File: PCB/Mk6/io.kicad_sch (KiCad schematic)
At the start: 7 parts, among them J10 PortA: 5V PA0 PA1 PA2 PA3 PA4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, J26 Conn_01x12, J27 Conn_01x12, J4 PortB: 5V PB0 PB1 PB2 PB3 PB4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, U25 74LS573, U26 74LS574, U6 R6522

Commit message: save point
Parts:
- added J5: DISPLAY, Connector_PinSocket_2.54mm:PinSocket_1x32_P2.54mm_Vertical, symbol Connector_Generic:Conn_01x32
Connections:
- net +5V: now also J5.18 (Pin_18)
- net A0: now also J5.20 (Pin_20)
- net A1: now also J5.21 (Pin_21)
- net A2: now also J5.22 (Pin_22)
- net A3: now also J5.23 (Pin_23)
- net Clk2: now also J5.7 (Pin_7)
- net D0: now also J5.10 (Pin_10)
- net D1: now also J5.11 (Pin_11)
- net D2: now also J5.12 (Pin_12)
- net D3: now also J5.13 (Pin_13)
- net D4: now also J5.14 (Pin_14)
- net D5: now also J5.15 (Pin_15)
- net D6: now also J5.16 (Pin_16)
- net D7: now also J5.17 (Pin_17)
- net GND: now also J5.19 (Pin_19)
- net R~{W}: now also J5.4 (Pin_4)
- net ~{IRQ}: now also J5.8 (Pin_8)
- net ~{RST}: now also J5.5 (Pin_5)
- net ~{OUT}: now reaches J27.10 (Pin_10), U26.11 (Cp)
- net ~{KEY}: now reaches J26.10 (Pin_10), U25.1 (~{OE})
- new net A10: J5.30 (Pin_30)
- new net A11: J5.31 (Pin_31)
- new net A12: J5.32 (Pin_32)
- new net A4: J5.24 (Pin_24)
- new net A5: J5.25 (Pin_25)
- new net A6: J5.26 (Pin_26)
- new net A7: J5.27 (Pin_27)
- new net A8: J5.28 (Pin_28)
- new net A9: J5.29 (Pin_29)
- new net DISP: J5.1 (Pin_1)
- new net RDY: J5.6 (Pin_6)
- new net ~{NMI}: J5.9 (Pin_9)
- new net ~{RD}: J5.3 (Pin_3)
- new net ~{WR}: J5.2 (Pin_2)

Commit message: save
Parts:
- added R3, R5: R_Small_US, Resistor_THT:R_Axial_DIN0204_L3.6mm_D1.6mm_P7.62mm_Horizontal, symbol Device:R_Small_US
- J7: renamed from J26; value Conn_01x12 -> Input Port; footprint Connector_PinHeader_1.00mm:PinHeader_1x12_P1.00mm_Vertical -> Connector_PinHeader_2.54mm:PinHeader_1x12_P2.54mm_Vertical
- J8: renamed from J27; value Conn_01x12 -> Output Port; footprint Connector_PinHeader_1.00mm:PinHeader_1x12_P1.00mm_Vertical -> Connector_PinHeader_2.54mm:PinHeader_1x12_P2.54mm_Vertical
- renumbered J5 to J10, J10 to J5, J4 to J6, U6 to U10, U25 to U11, U26 to U12
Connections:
- net +5V: now also R5.1
- net A0: now also J10.32 (Pin_32); no longer J10.20 (Pin_20)
- net A1: now also J10.31 (Pin_31); no longer J10.21 (Pin_21)
- net A10: now also J10.22 (Pin_22); no longer J10.30 (Pin_30)
- net A11: now also J10.21 (Pin_21); no longer J10.31 (Pin_31)
- net A12: now also J10.20 (Pin_20); no longer J10.32 (Pin_32)
- net A2: now also J10.30 (Pin_30); no longer J10.22 (Pin_22)
- net A3: now also J10.29 (Pin_29); no longer J10.23 (Pin_23)
- net A4: now also J10.28 (Pin_28); no longer J10.24 (Pin_24)
- net A5: now also J10.27 (Pin_27); no longer J10.25 (Pin_25)
- net A7: now also J10.25 (Pin_25); no longer J10.27 (Pin_27)
- net A8: now also J10.24 (Pin_24); no longer J10.28 (Pin_28)
- net A9: now also J10.23 (Pin_23); no longer J10.29 (Pin_29)
- net GND: now also R3.1
- net ~{OutEn}: now reaches J8.11 (Pin_11), U12.1 (~{OE})
- net ~{OutEn}: now also R3.2
- net ~{Hold}/Follow: now reaches J7.11 (Pin_11), U11.11 (Load)
- net ~{Hold}/Follow: now also R5.2
- net ~{KEY} renamed ~{IN}
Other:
- moved on the sheet: J10

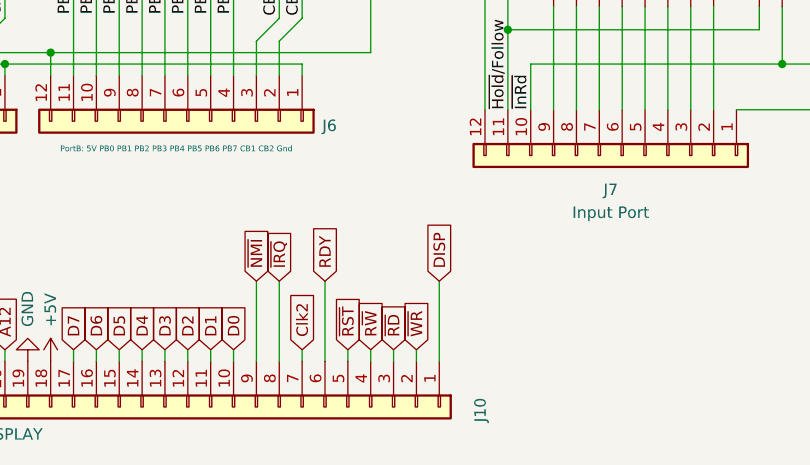
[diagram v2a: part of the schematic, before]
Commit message: all done, pre-clk div
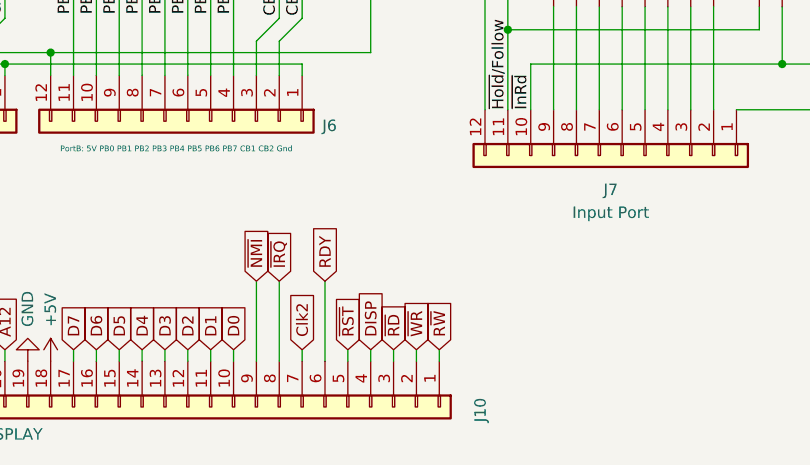
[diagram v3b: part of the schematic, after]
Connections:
- net DISP: now also J10.4 (Pin_4); no longer J10.1 (Pin_1)
- net R~{W}: now also J10.1 (Pin_1); no longer J10.4 (Pin_4)

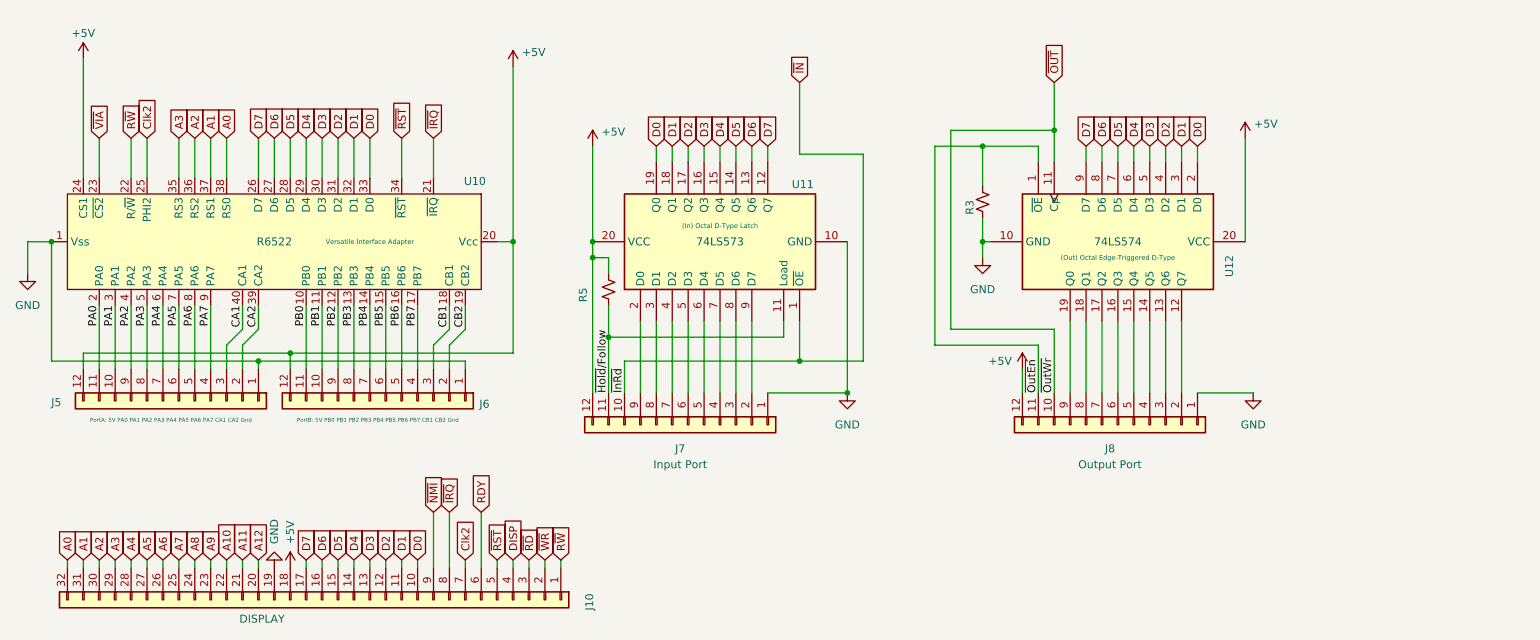
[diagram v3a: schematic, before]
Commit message: Added 3-8 IO, extra GAL out, attachment point for !RAM
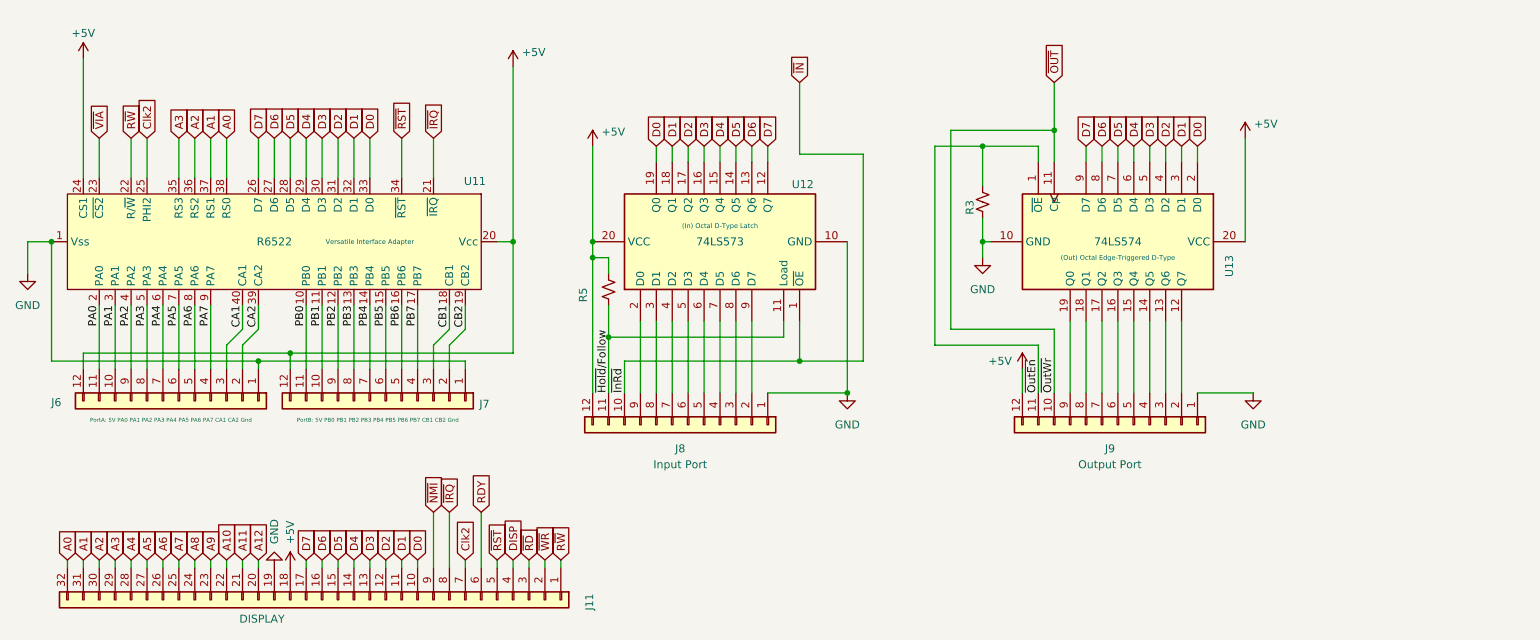
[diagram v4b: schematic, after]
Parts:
- renumbered J10 to J11, J5 to J6, J6 to J7, J7 to J8, J8 to J9, U10 to U11, U11 to U12, U12 to U13
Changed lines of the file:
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@@
 		(dnp no)
 		(fields_autoplaced yes)
-		(property "Reference" "J8"
+		(property "Reference" "J9"
 			(at 191.77 91.44 90)
 			(effects
@@
 			(project ""
 				(path "/d41350ce-2040-418d-ae11-f076a5474776/991bdc6c-c9f2-46dc-9106-bb77d701fb18"
-					(reference "J8")
+					(reference "J9")
 					(unit 1)
 				)
@@
 		(dnp no)
 		(fields_autoplaced yes)
-		(property "Reference" "U12"
+		(property "Reference" "U13"
 			(at 210.82 60.5633 0)
 			(effects
@@
 			(project ""
 				(path "/d41350ce-2040-418d-ae11-f076a5474776/991bdc6c-c9f2-46dc-9106-bb77d701fb18"
-					(reference "U12")
+					(reference "U13")
 					(unit 1)
 				)
@@
 		(dnp no)
 		(fields_autoplaced yes)
-		(property "Reference" "#PWR037"
+		(property "Reference" "#PWR038"
 			(at 60.96 114.3 0)
 			(effects
@@
 			(project "Mk6"
 				(path "/d41350ce-2040-418d-ae11-f076a5474776/991bdc6c-c9f2-46dc-9106-bb77d701fb18"
-					(reference "#PWR037")
+					(reference "#PWR038")
 					(unit 1)
 				)
@@
 		(on_board yes)
 		(dnp no)
-		(property "Reference" "J6"
+		(property "Reference" "J7"
 			(at 91.948 84.328 90)
 			(effects
@@
 			(project "Mk6"
 				(path "/d41350ce-2040-418d-ae11-f076a5474776/991bdc6c-c9f2-46dc-9106-bb77d701fb18"
-					(reference "J6")
+					(reference "J7")
 					(unit 1)
 				)
@@
 		(on_board yes)
 		(dnp no)
-		(property "Reference" "#PWR023"
+		(property "Reference" "#PWR024"
 			(at 27.94 33.02 0)
 			(effects
@@
 			(project "Mk6"
 				(path "/d41350ce-2040-418d-ae11-f076a5474776/991bdc6c-c9f2-46dc-9106-bb77d701fb18"
-					(reference "#PWR023")
+					(reference "#PWR024")
 					(unit 1)
 				)
@@
 		(on_board yes)
 		(dnp no)
-		(property "Reference" "#PWR024"
+		(property "Reference" "#PWR025"
 			(at 96.52 34.29 0)
 			(effects
@@
 			(project "Mk6"
 				(path "/d41350ce-2040-418d-ae11-f076a5474776/991bdc6c-c9f2-46dc-9106-bb77d701fb18"
-					(reference "#PWR024")
+					(reference "#PWR025")
 					(unit 1)
 				)
@@
 		(on_board yes)
 		(dnp no)
-		(property "Reference" "#PWR025"
+		(property "Reference" "#PWR026"
 			(at 213.36 45.72 0)
 			(effects
@@
 			(project "Mk6"
 				(path "/d41350ce-2040-418d-ae11-f076a5474776/991bdc6c-c9f2-46dc-9106-bb77d701fb18"
-					(reference "#PWR025")
+					(reference "#PWR026")
 					(unit 1)
 				)
@@
 		(dnp no)
 		(fields_autoplaced yes)
-		(property "Reference" "#PWR030"
+		(property "Reference" "#PWR031"
 			(at 19.05 69.85 0)
 			(effects
@@
 			(project "Mk6"
 				(path "/d41350ce-2040-418d-ae11-f076a5474776/991bdc6c-c9f2-46dc-9106-bb77d701fb18"
-					(reference "#PWR030")
+					(reference "#PWR031")
 					(unit 1)
 				)
@@
 		(on_board yes)
 		(dnp no)
-		(property "Reference" "#PWR027"
+		(property "Reference" "#PWR028"
 			(at 109.22 46.99 0)
 			(effects
@@
 			(project "Mk6"
 				(path "/d41350ce-2040-418d-ae11-f076a5474776/991bdc6c-c9f2-46dc-9106-bb77d701fb18"
-					(reference "#PWR027")
+					(reference "#PWR028")
 					(unit 1)
 				)
@@
 		(on_board yes)
 		(dnp no)
-		(property "Reference" "#PWR032"
+		(property "Reference" "#PWR033"
 			(at 177.8 82.55 0)
 			(effects
@@
 			(project "Mk6"
 				(path "/d41350ce-2040-418d-ae11-f076a5474776/991bdc6c-c9f2-46dc-9106-bb77d701fb18"
-					(reference "#PWR032")
+					(reference "#PWR033")
 					(unit 1)
 				)
@@
 		(dnp no)
 		(fields_autoplaced yes)
-		(property "Reference" "#PWR036"
+		(property "Reference" "#PWR037"
 			(at 58.42 104.14 0)
 			(effects
@@
 			(project "Mk6"
 				(path "/d41350ce-2040-418d-ae11-f076a5474776/991bdc6c-c9f2-46dc-9106-bb77d701fb18"
-					(reference "#PWR036")
+					(reference "#PWR037")
 					(unit 1)
 				)
@@
 		(dnp no)
 		(fields_autoplaced yes)
-		(property "Reference" "#PWR034"
+		(property "Reference" "#PWR035"
 			(at 149.86 88.9 0)
 			(effects
@@
 			(project "Mk6"
 				(path "/d41350ce-2040-418d-ae11-f076a5474776/991bdc6c-c9f2-46dc-9106-bb77d701fb18"
-					(reference "#PWR034")
+					(reference "#PWR035")
 					(unit 1)
 				)
@@
 		(on_board yes)
 		(dnp no)
-		(property "Reference" "U11"
+		(property "Reference" "U12"
 			(at 142.748 49.276 90)
 			(effects
@@
 			(project ""
 				(path "/d41350ce-2040-418d-ae11-f076a5474776/991bdc6c-c9f2-46dc-9106-bb77d701fb18"
-					(reference "U11")
+					(reference "U12")
 					(unit 1)
 				)
@@
 		(dnp no)
 		(fields_autoplaced yes)
-		(property "Reference" "#PWR028"
+		(property "Reference" "#PWR029"
 			(at 171.45 67.31 0)
 			(effects
@@
 			(project "Mk6"
 				(path "/d41350ce-2040-418d-ae11-f076a5474776/991bdc6c-c9f2-46dc-9106-bb77d701fb18"
-					(reference "#PWR028")
+					(reference "#PWR029")
 					(unit 1)
 				)
@@
 		(dnp no)
 		(fields_autoplaced yes)
-		(property "Reference" "#PWR035"
+		(property "Reference" "#PWR036"
 			(at 214.63 88.9 0)
 			(effects
@@
 			(project "Mk6"
 				(path "/d41350ce-2040-418d-ae11-f076a5474776/991bdc6c-c9f2-46dc-9106-bb77d701fb18"
-					(reference "#PWR035")
+					(reference "#PWR036")
 					(unit 1)
 				)
@@
 		(dnp no)
 		(fields_autoplaced yes)
-		(property "Reference" "J7"
+		(property "Reference" "J8"
 			(at 123.19 91.44 90)
 			(effects
@@
 			(project ""
 				(path "/d41350ce-2040-418d-ae11-f076a5474776/991bdc6c-c9f2-46dc-9106-bb77d701fb18"
-					(reference "J7")
+					(reference "J8")
 					(unit 1)
 				)
@@
 		(on_board yes)
 		(dnp no)
-		(property "Reference" "J10"
+		(property "Reference" "J11"
 			(at 108.712 114.554 0)
 			(effects
@@
 			(project "Mk6"
 				(path "/d41350ce-2040-418d-ae11-f076a5474776/991bdc6c-c9f2-46dc-9106-bb77d701fb18"
-					(reference "J10")
+					(reference "J11")
 					(unit 1)
 				)
@@
 		(on_board yes)
 		(dnp no)
-		(property "Reference" "J5"
+		(property "Reference" "J6"
 			(at 23.622 84.074 90)
 			(effects
@@
 			(project "Mk6"
 				(path "/d41350ce-2040-418d-ae11-f076a5474776/991bdc6c-c9f2-46dc-9106-bb77d701fb18"
-					(reference "J5")
+					(reference "J6")
 					(unit 1)
 				)
@@
 		(on_board yes)
 		(dnp no)
-		(property "Reference" "U10"
+		(property "Reference" "U11"
 			(at 90.424 48.768 90)
 			(effects
@@
 			(project "Mk6"
 				(path "/d41350ce-2040-418d-ae11-f076a5474776/991bdc6c-c9f2-46dc-9106-bb77d701fb18"
-					(reference "U10")
-					(unit 1)
-				)
+					(reference "U11")
+					(unit 1)
+				)

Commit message: cleanup
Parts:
- J6: value PortA: 5V PA0 PA1 PA2 PA3 PA4 PA5 PA6 PA7 CA1 CA2 Gnd -> PortA: GND CA2 CA1 PA7 PA6 PA5 PA4 PA3 PA2 PA1 PA0 5v
- J7: value PortB: 5V PB0 PB1 PB2 PB3 PB4 PB5 PB6 PB7 CB1 CB2 Gnd -> PortB: GND CB2 CB1 PB7 PB6 PB5 PB4 PB3 PB2 PB1 PB0 5v
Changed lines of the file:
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@@
 			)
 		)
-		(property "Value" "PortB: 5V PB0 PB1 PB2 PB3 PB4 PB5 PB6 PB7 CB1 CB2 Gnd"
+		(property "Value" "PortB: GND CB2 CB1 PB7 PB6 PB5 PB4 PB3 PB2 PB1 PB0 5v"
 			(at 74.93 86.868 90)
 			(effects
@@
 			)
 		)
-		(property "Value" "PortA: 5V PA0 PA1 PA2 PA3 PA4 PA5 PA6 PA7 CA1 CA2 Gnd"
+		(property "Value" "PortA: GND CA2 CA1 PA7 PA6 PA5 PA4 PA3 PA2 PA1 PA0 5v"
 			(at 41.91 86.868 90)
 			(effects
